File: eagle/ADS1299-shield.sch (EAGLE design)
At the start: 133 parts, among them IC1 ADS1299IPAG, IC2 TPS72325DBVT, IC3 TPS73225DBVT, IC5 24AA256UID, IC6 TPS60403DBVT, IC7 OPA376DBV, IC8 OPA376DBV, IC9 TXS0102DCTR, J16 EXTERNAL_SYNC, J8 Electrode Connector, U2 TXB0108PWR, U3 TXB0108PWR

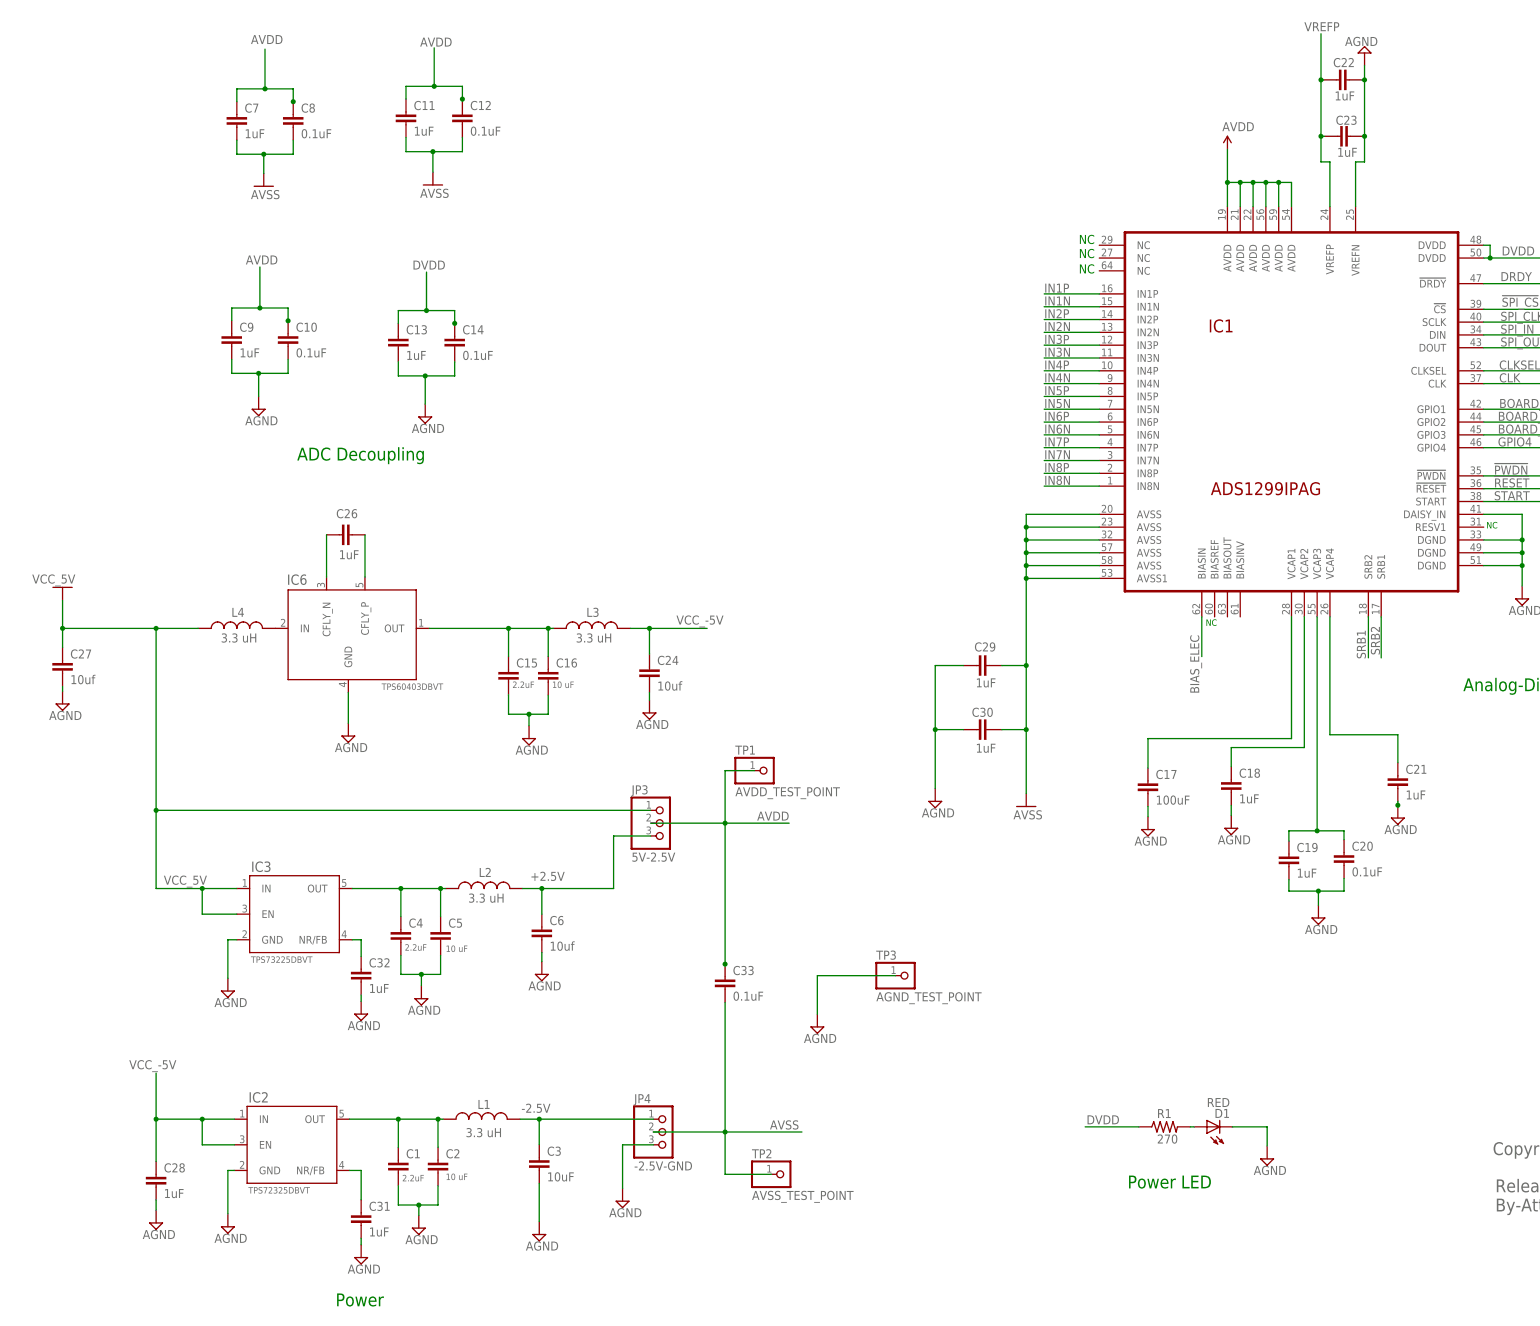
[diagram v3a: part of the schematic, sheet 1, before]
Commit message: fixed many errors found by rechecking ADS1299 Eval Board schematic. Rerouted board. Passes ERC and DRC.
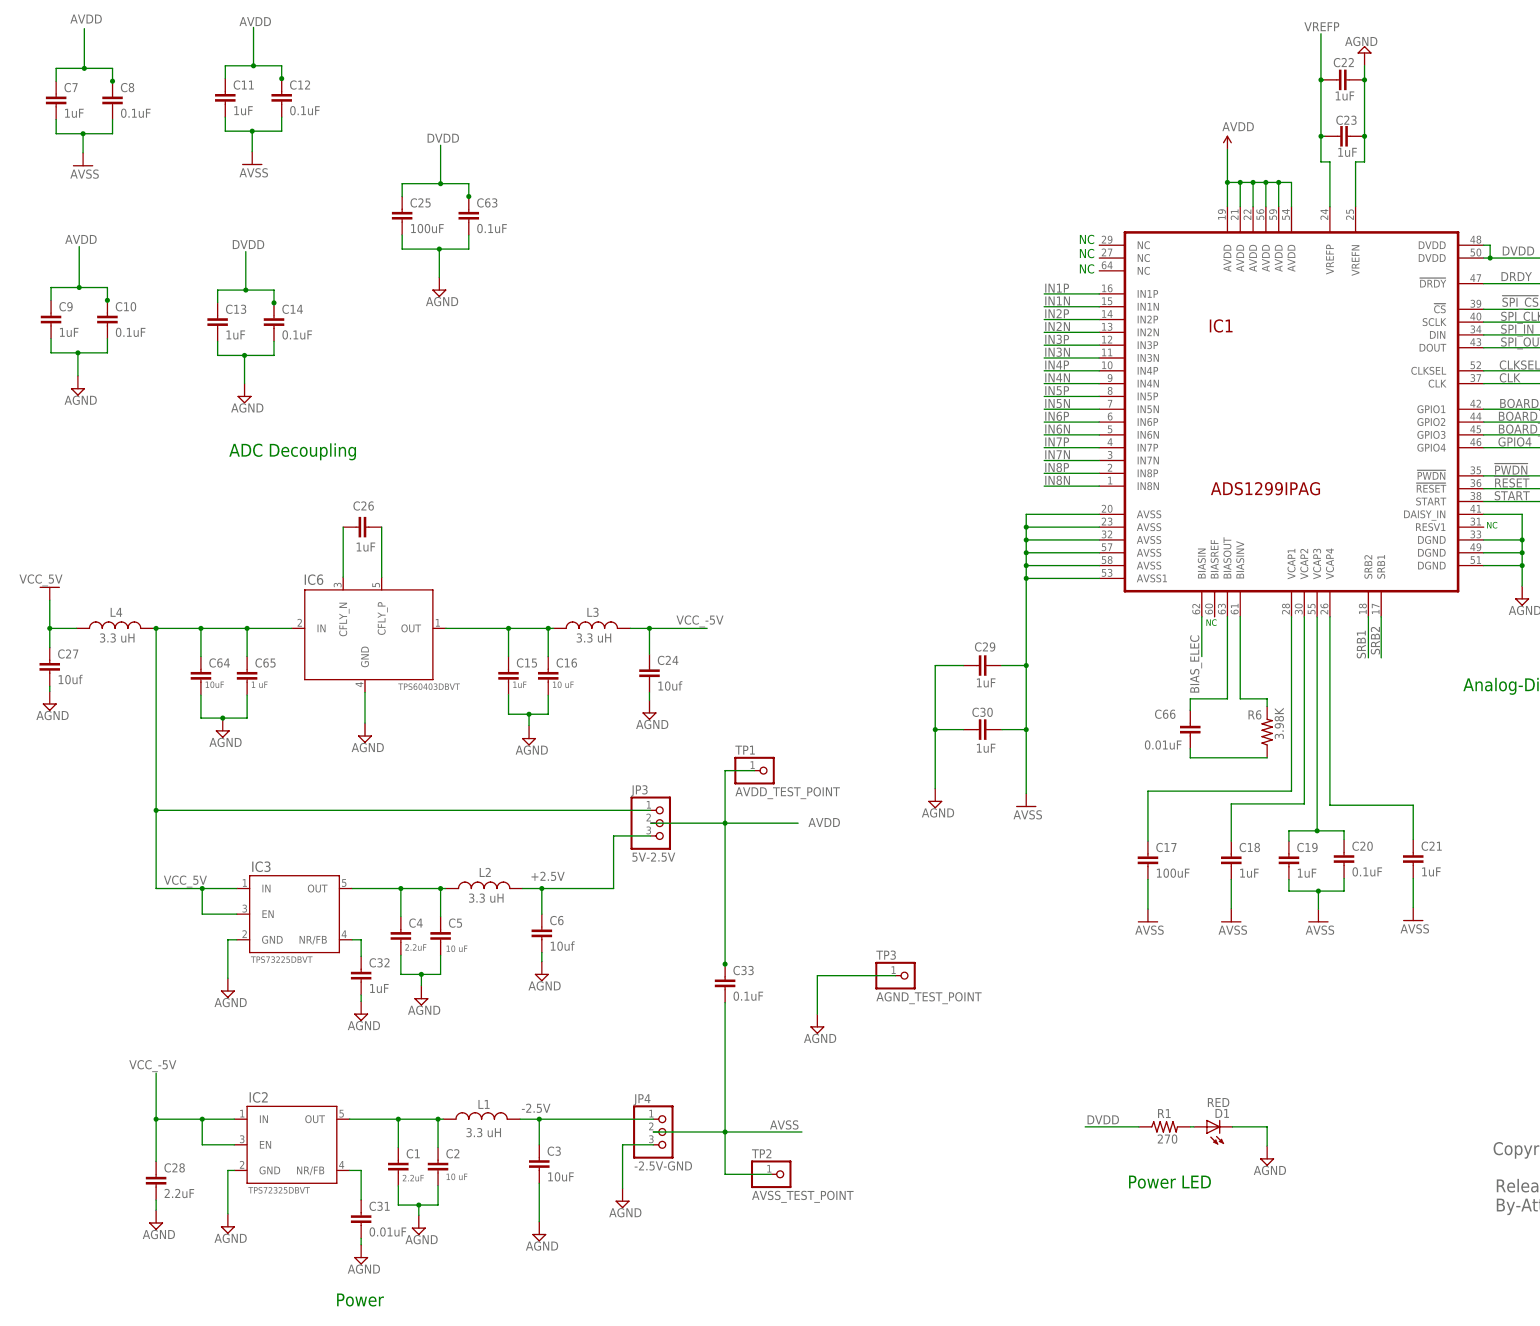
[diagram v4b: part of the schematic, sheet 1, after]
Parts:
- added C25: 100uF, SparkFun-Passives:CAP1210
- added C63: 0.1uF, SparkFun-Passives:CAP0603-CAP
- added C64: 10uF, SparkFun-Passives:CAP0603-CAP
- added C65: 1 uF, SparkFun-Passives:CAP0603-CAP
- added C66: 0.01uF, SparkFun-Passives:CAP0603-CAP
- added R6: 3.98K, SparkFun-Passives:RESISTOR0603-RES
- C15: value 2.2uF -> 1uF
- C28: value 1uF -> 2.2uF
- C31: value 1uF -> 0.01uF
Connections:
- removed net N$66: JP14.4
- new net N$22: C66.2, R6.1
- new net N$25: C66.1, IC1.BIASOUT
- net AGND: now also C25.2, C27.1, C63.2, C64.2, C65.2, L4.1; no longer C17.2, C18.2, C19.2, C20.2, C21.2
- net AVSS: now also C17.2, C18.2, C19.2, C20.2, C21.2
- net DVDD: now also C25.1, C63.1, JP14.4
- net N$12: now also IC1.BIASINV, R6.2; no longer IC6.IN, L4.2
- net VCC_5V: now also C64.1, C65.1, IC6.IN, L4.2; no longer C27.1, L4.1
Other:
- moved on the sheet: C10, C11, C12, C13, C14, C17, C18, C21, C26, C27, C7, C8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

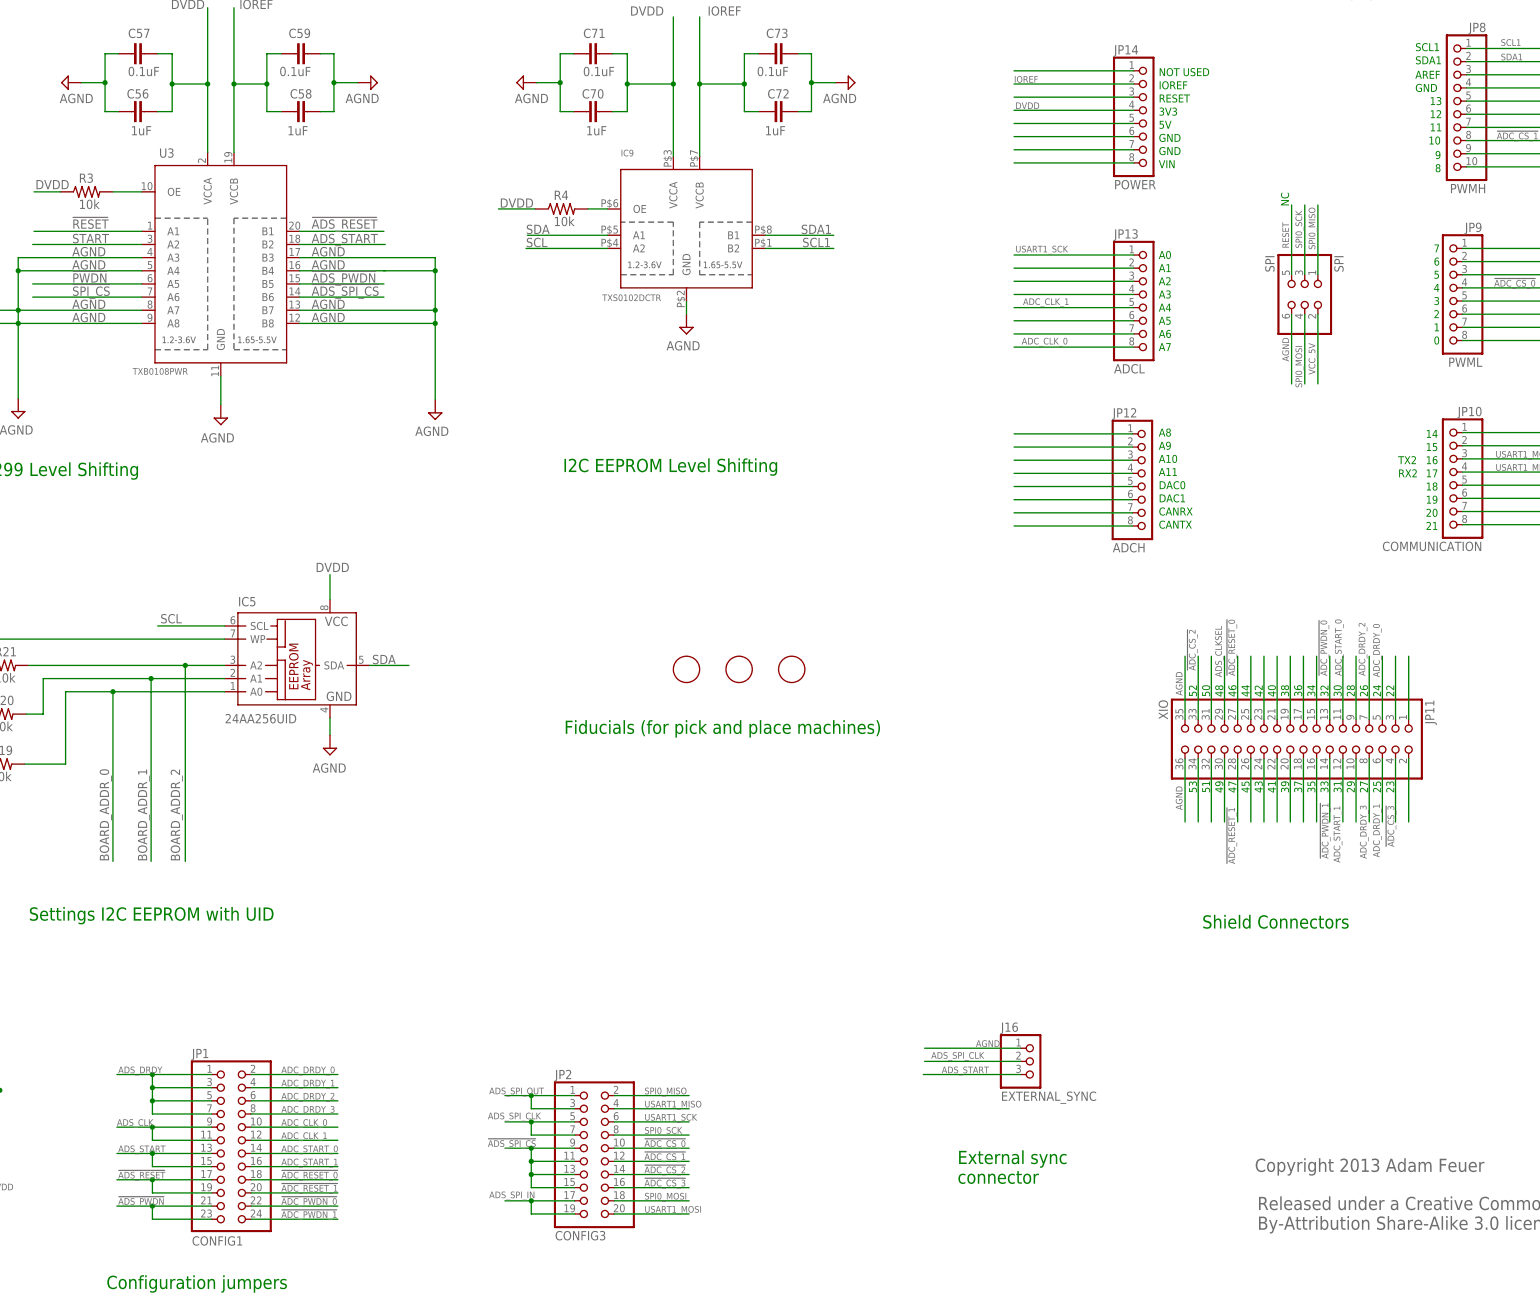
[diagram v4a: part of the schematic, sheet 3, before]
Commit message: fixes to schematic and board - created VCC_5V_FILTERED net to correct current draw problem; changed inductors to 0805 to fix current flow problem
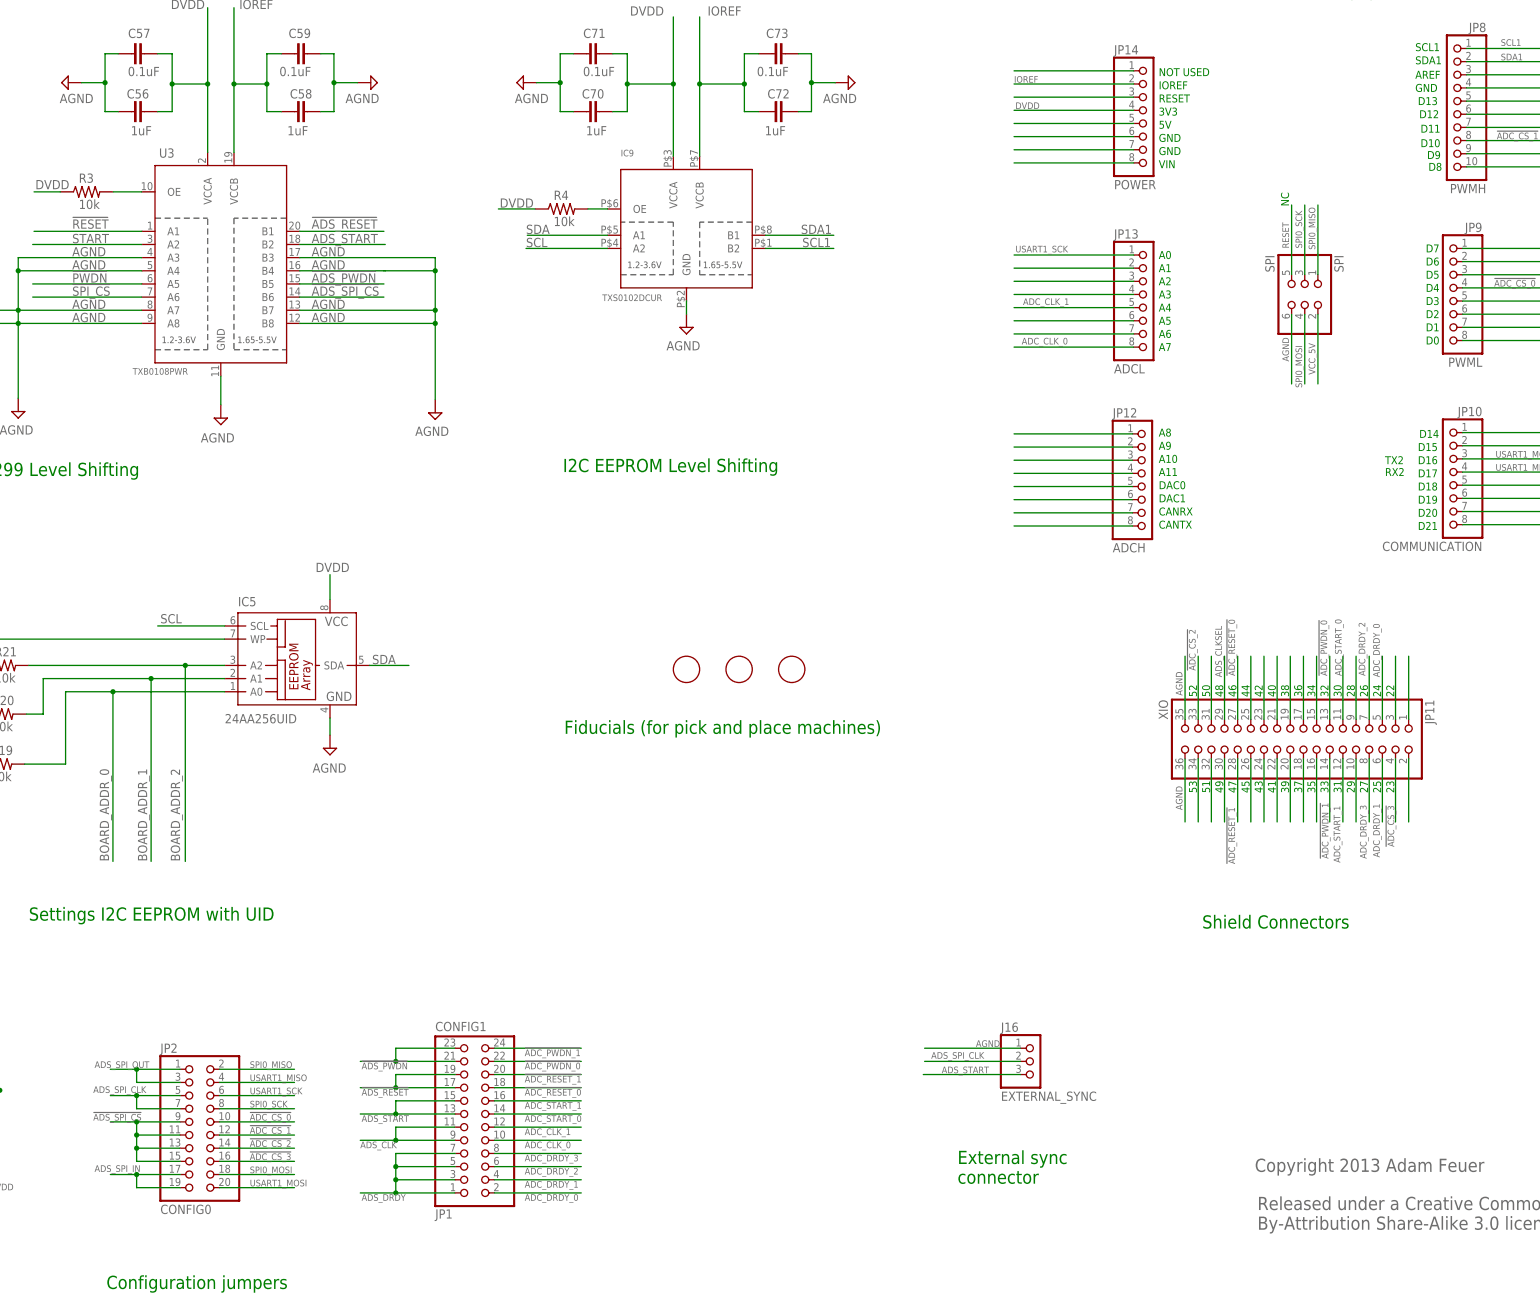
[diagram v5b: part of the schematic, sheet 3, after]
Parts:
- IC9: value TXS0102DCTR -> TXS0102DCUR
- JP2: value CONFIG3 -> CONFIG0
- L1, L2, L3, L4: device SparkFun-Passives:INDUCTOR0603 -> SparkFun-Passives:INDUCTOR0805
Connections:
- new net VCC_5V_FILTERED: C64.1, C65.1, IC3.EN, IC3.IN, IC6.IN, JP3.1, L4.2
- net AGND: no longer C27.1, L4.1
- net VCC_5V: now also C27.1, L4.1; no longer C64.1, C65.1, IC3.EN, IC3.IN, IC6.IN, JP3.1, L4.2
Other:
- note added: "D0"
- note added: "D1"
- note added: "D10"
- note added: "D11"
- note added: "D12"
- note added: "D13"
- note added: "D14"
- note added: "D15"
- note added: "D16"
- note added: "D17"
- note added: "D18"
- note added: "D19"
- note added: "D2"
- note added: "D20"
- note added: "D21"
- note added: "D3"
- note added: "D4"
- note added: "D5"
- note added: "D6"
- note added: "D7"
- note added: "D8"
- note added: "D9"
- note removed: "0"
- note removed: "1"
- note removed: "10"
- note removed: "11"
- note removed: "12"
- note removed: "13"
- note removed: "14"
- note removed: "15"
- note removed: "16"
- note removed: "17"
- note removed: "18"
- note removed: "19"
- note removed: "2"
- note removed: "20"
- note removed: "21"
- note removed: "3"
- note removed: "4"
- note removed: "5"
- note removed: "6"
- note removed: "7"
- note removed: "8"
- note removed: "9"
- moved on the sheet: JP1, JP2
